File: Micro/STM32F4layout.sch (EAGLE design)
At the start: 38 parts, among them Q1 ASF, U1 LM1085IS-3.3

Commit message: Finished Power Layout, added pin header, added USB
finished list from Luke/Sam Conversation
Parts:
- removed SV2, SV3: (no value), Connectors:FE18-2
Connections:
- removed net N$8: RN1A.2
- removed net N$9: RN1B.2
- new net ETH_MDC: SV1.31
- net +3V3: now also SV1.4, U1.OUT, U1.VOUT; no longer C14.2
- net +5V: now also SV1.2
- net CAN1_RX: now also RN1A.2, SV1.1
- net CAN1_TX: now also RN1B.2, SV1.3
- net CAN2_RX: now also SV1.5
- net CAN2_TX: now also SV1.7
- net ETH_CRS_DV: now also SV1.25
- net ETH_MDIO: now also SV1.23
- net ETH_REF_CLK: now also SV1.21
- net ETH_RXD0: now also SV1.27
- net ETH_RXD1: now also SV1.29
- net ETH_TXD0: now also SV1.9
- net ETH_TXD1: now also SV1.11
- net ETH_TX_EN: now also SV1.13
- net GND: now also SV1.12, SV1.6, SV1.8, U1.ADJ/GND
- net I2C_SCL: now also SV1.17
- net I2C_SDA: now also SV1.19
- net OSC_IN: now also SV1.15
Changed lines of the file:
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@@
 <part name="GND16" library="SparkFun-Aesthetics" deviceset="GND" device=""/>
 <part name="SV1" library="Connectors" deviceset="FE18-2" device=""/>
-<part name="SV2" library="Connectors" deviceset="FE18-2" device=""/>
-<part name="SV3" library="Connectors" deviceset="FE18-2" device=""/>
+<part name="GND17" library="SparkFun-Aesthetics" deviceset="GND" device=""/>
+<part name="+3V8" library="supply1" deviceset="+3V3" device=""/>
 </parts>
 <sheets>
@@
 <instance part="GND16" gate="1" x="111.76" y="-121.92"/>
 <instance part="SV1" gate="G$1" x="160.02" y="-162.56"/>
-<instance part="SV2" gate="G$1" x="160.02" y="-215.9"/>
-<instance part="SV3" gate="G$1" x="160.02" y="-269.24"/>
+<instance part="GND17" gate="1" x="-439.42" y="-261.62"/>
+<instance part="+3V8" gate="G$1" x="-386.08" y="-226.06"/>
 </instances>
 <busses>
@@
 <junction x="106.68" y="-114.3"/>
 </segment>
+<segment>
+<pinref part="GND17" gate="1" pin="GND"/>
+<pinref part="U1" gate="A" pin="ADJ/GND"/>
+<wire x1="-439.42" y1="-259.08" x2="-439.42" y2="-248.92" width="0.1524" layer="91"/>
+</segment>
+<segment>
+<pinref part="SV1" gate="G$1" pin="6"/>
+<wire x1="167.64" y1="-180.34" x2="172.72" y2="-180.34" width="0.1524" layer="91"/>
+<label x="170.18" y="-180.34" size="1.778" layer="95"/>
+</segment>
+<segment>
+<pinref part="SV1" gate="G$1" pin="8"/>
+<wire x1="167.64" y1="-177.8" x2="172.72" y2="-177.8" width="0.1524" layer="91"/>
+<label x="170.18" y="-177.8" size="1.778" layer="95"/>
+</segment>
+<segment>
+<wire x1="165.1" y1="-175.26" x2="172.72" y2="-175.26" width="0.1524" layer="91"/>
+<label x="170.18" y="-175.26" size="1.778" layer="95"/>
+</segment>
+<segment>
+<pinref part="SV1" gate="G$1" pin="12"/>
+<wire x1="167.64" y1="-172.72" x2="172.72" y2="-172.72" width="0.1524" layer="91"/>
+<label x="170.18" y="-172.72" size="1.778" layer="95"/>
+</segment>
 </net>
 <net name="+3V3" class="0">
@@
 <junction x="-259.08" y="-20.32"/>
 <pinref part="U$1" gate="G$6" pin="VDD3"/>
-<pinref part="C14" gate="G$1" pin="2"/>
 <wire x1="-264.16" y1="-15.24" x2="-259.08" y2="-15.24" width="0.1524" layer="91"/>
-<wire x1="-259.08" y1="-15.24" x2="-238.76" y2="-15.24" width="0.1524" layer="91"/>
-<wire x1="-238.76" y1="-15.24" x2="-238.76" y2="-2.54" width="0.1524" layer="91"/>
-<junction x="-238.76" y="-15.24"/>
+<wire x1="-259.08" y1="-15.24" x2="-220.98" y2="-15.24" width="0.1524" layer="91"/>
 <wire x1="-259.08" y1="-20.32" x2="-259.08" y2="-15.24" width="0.1524" layer="91"/>
 <junction x="-259.08" y="-15.24"/>
@@
 <junction x="-261.62" y="-5.08"/>
 <wire x1="-259.08" y1="-10.16" x2="-259.08" y2="-5.08" width="0.1524" layer="91"/>
-<wire x1="-238.76" y1="-15.24" x2="-220.98" y2="-15.24" width="0.1524" layer="91"/>
 <pinref part="C13" gate="G$1" pin="1"/>
 <wire x1="-259.08" y1="-20.32" x2="-241.3" y2="-20.32" width="0.1524" layer="91"/>
@@
 <wire x1="88.9" y1="86.36" x2="88.9" y2="83.82" width="0.1524" layer="91"/>
 </segment>
+<segment>
+<pinref part="+3V8" gate="G$1" pin="+3V3"/>
+<wire x1="-398.78" y1="-243.84" x2="-386.08" y2="-243.84" width="0.1524" layer="91"/>
+<pinref part="U1" gate="A" pin="VOUT"/>
+<wire x1="-386.08" y1="-243.84" x2="-386.08" y2="-228.6" width="0.1524" layer="91"/>
+<wire x1="-398.78" y1="-246.38" x2="-386.08" y2="-246.38" width="0.1524" layer="91"/>
+<wire x1="-386.08" y1="-246.38" x2="-386.08" y2="-243.84" width="0.1524" layer="91"/>
+<pinref part="U1" gate="A" pin="OUT"/>
+<wire x1="-401.32" y1="-243.84" x2="-398.78" y2="-243.84" width="0.1524" layer="91"/>
+<junction x="-398.78" y="-243.84"/>
+</segment>
+<segment>
+<pinref part="SV1" gate="G$1" pin="4"/>
+<wire x1="167.64" y1="-182.88" x2="172.72" y2="-182.88" width="0.1524" layer="91"/>
+<label x="170.18" y="-182.88" size="1.778" layer="95"/>
+</segment>
 </net>
 <net name="N$3" class="0">
@@
 <label x="-43.18" y="78.74" size="1.778" layer="95"/>
 </segment>
+<segment>
+<pinref part="SV1" gate="G$1" pin="17"/>
+<wire x1="152.4" y1="-165.1" x2="149.86" y2="-165.1" width="0.1524" layer="91"/>
+<label x="142.24" y="-165.1" size="1.778" layer="95"/>
+</segment>
 </net>
 <net name="I2C_SDA" class="0">
@@
 <label x="93.98" y="73.66" size="1.778" layer="95"/>
 </segment>
+<segment>
+<pinref part="SV1" gate="G$1" pin="19"/>
+<wire x1="152.4" y1="-162.56" x2="149.86" y2="-162.56" width="0.1524" layer="91"/>
+<label x="142.24" y="-162.56" size="1.778" layer="95"/>
+</segment>
 </net>
 <net name="N$6" class="0">
@@
 <pinref part="RN1" gate="A" pin="1"/>
 <wire x1="-485.14" y1="-271.78" x2="-464.82" y2="-271.78" width="0.1524" layer="91"/>
-</segment>
-</net>
-<net name="N$8" class="0">
-<segment>
-<pinref part="RN1" gate="A" pin="2"/>
-<wire x1="-454.66" y1="-271.78" x2="-452.12" y2="-271.78" width="0.1524" layer="91"/>
-</segment>
-</net>
-<net name="N$9" class="0">
-<segment>
-<pinref part="RN1" gate="B" pin="2"/>
-<wire x1="-454.66" y1="-276.86" x2="-452.12" y2="-276.86" width="0.1524" layer="91"/>
 </segment>
 </net>
@@
 <junction x="-464.82" y="-243.84"/>
 </segment>
+<segment>
+<pinref part="SV1" gate="G$1" pin="2"/>
+<wire x1="167.64" y1="-185.42" x2="172.72" y2="-185.42" width="0.1524" layer="91"/>
+<label x="170.18" y="-185.42" size="1.778" layer="95"/>
+</segment>
 </net>
 <net name="N$5" class="0">
@@
 <wire x1="-60.96" y1="-160.02" x2="-43.18" y2="-160.02" width="0.1524" layer="91"/>
 <label x="-55.88" y="-160.02" size="1.778" layer="95"/>
+</segment>
+<segment>
+<pinref part="SV1" gate="G$1" pin="15"/>
+<wire x1="152.4" y1="-167.64" x2="149.86" y2="-167.64" width="0.1524" layer="91"/>
+<label x="142.24" y="-167.64" size="1.778" layer="95"/>
 </segment>
 </net>
@@
 <label x="-63.5" y="58.42" size="1.778" layer="95"/>
 </segment>
+<segment>
+<pinref part="RN1" gate="B" pin="2"/>
+<wire x1="-454.66" y1="-276.86" x2="-452.12" y2="-276.86" width="0.1524" layer="91"/>
+</segment>
+<segment>
+<pinref part="SV1" gate="G$1" pin="3"/>
+<wire x1="152.4" y1="-182.88" x2="149.86" y2="-182.88" width="0.1524" layer="91"/>
+<label x="142.24" y="-182.88" size="1.778" layer="95"/>
+</segment>
 </net>
 <net name="N$13" class="0">
@@
 <label x="-66.04" y="114.3" size="1.778" layer="95"/>
 </segment>
+<segment>
+<pinref part="SV1" gate="G$1" pin="21"/>
+<wire x1="152.4" y1="-160.02" x2="149.86" y2="-160.02" width="0.1524" layer="91"/>
+<label x="137.16" y="-160.02" size="1.778" layer="95"/>
+</segment>
 </net>
 <net name="ETH_MDIO" class="0">
@@
 <label x="-66.04" y="109.22" size="1.778" layer="95"/>
 </segment>
+<segment>
+<pinref part="SV1" gate="G$1" pin="23"/>
+<wire x1="152.4" y1="-157.48" x2="149.86" y2="-157.48" width="0.1524" layer="91"/>
+<label x="139.7" y="-157.48" size="1.778" layer="95"/>
+</segment>
 </net>
 <net name="ETH_CRS_DV" class="0">
@@
 <label x="-68.58" y="83.82" size="1.778" layer="95"/>
 </segment>
+<segment>
+<pinref part="SV1" gate="G$1" pin="25"/>
+<wire x1="152.4" y1="-154.94" x2="149.86" y2="-154.94" width="0.1524" layer="91"/>
+<label x="137.16" y="-154.94" size="1.778" layer="95"/>
+</segment>
 </net>
 <net name="ETH_RXD0" class="0">
@@
 <label x="73.66" y="99.06" size="1.778" layer="95"/>
 </segment>
+<segment>
+<pinref part="SV1" gate="G$1" pin="27"/>
+<wire x1="152.4" y1="-152.4" x2="149.86" y2="-152.4" width="0.1524" layer="91"/>
+<label x="139.7" y="-152.4" size="1.778" layer="95"/>
+</segment>
 </net>
 <net name="ETH_RXD1" class="0">
@@
 <label x="73.66" y="93.98" size="1.778" layer="95"/>
 </segment>
+<segment>
+<pinref part="SV1" gate="G$1" pin="29"/>
+<wire x1="152.4" y1="-149.86" x2="149.86" y2="-149.86" width="0.1524" layer="91"/>
+<label x="139.7" y="-149.86" size="1.778" layer="95"/>
+</segment>
 </net>
 <net name="BUCK_ON/OFF" class="0">
@@
 <label x="-58.42" y="-93.98" size="1.778" layer="95"/>
 </segment>
+<segment>
+<pinref part="SV1" gate="G$1" pin="13"/>
+<wire x1="152.4" y1="-170.18" x2="149.86" y2="-170.18" width="0.1524" layer="91"/>
+<label x="142.24" y="-170.18" size="1.778" layer="95"/>
+</segment>
 </net>
 <net name="ETH_TXD1" class="0">
@@
 <label x="-58.42" y="-104.14" size="1.778" layer="95"/>
 </segment>
+<segment>
+<pinref part="SV1" gate="G$1" pin="11"/>
+<wire x1="152.4" y1="-172.72" x2="149.86" y2="-172.72" width="0.1524" layer="91"/>
+<label x="142.24" y="-172.72" size="1.778" layer="95"/>
+</segment>
 </net>
 <net name="ETH_TXD0" class="0">
@@
 <label x="-58.42" y="-99.06" size="1.778" layer="95"/>
 </segment>
+<segment>
+<pinref part="SV1" gate="G$1" pin="9"/>
+<wire x1="152.4" y1="-175.26" x2="149.86" y2="-175.26" width="0.1524" layer="91"/>
+<label x="142.24" y="-175.26" size="1.778" layer="95"/>
+</segment>
 </net>
 <net name="CAN2_TX" class="0">
@@
 <label x="-93.98" y="-330.2" size="1.778" layer="95"/>
 </segment>
+<segment>
+<pinref part="SV1" gate="G$1" pin="7"/>
+<wire x1="152.4" y1="-177.8" x2="149.86" y2="-177.8" width="0.1524" layer="91"/>
+<label x="142.24" y="-177.8" size="1.778" layer="95"/>
+</segment>
 </net>
 <net name="CAN2_RX" class="0">
@@
 <label x="-93.98" y="-335.28" size="1.778" layer="95"/>
 </segment>
+<segment>
+<pinref part="SV1" gate="G$1" pin="5"/>
+<wire x1="152.4" y1="-180.34" x2="149.86" y2="-180.34" width="0.1524" layer="91"/>
+<label x="142.24" y="-180.34" size="1.778" layer="95"/>
+</segment>
 </net>
 <net name="CAN1_RX" class="0">
@@
 <label x="-96.52" y="-256.54" size="1.778" layer="95"/>
 </segment>
-</net>
+<segment>
+<pinref part="RN1" gate="A" pin="2"/>
+<wire x1="-454.66" y1="-271.78" x2="-452.12" y2="-271.78" width="0.1524" layer="91"/>
+</segment>
+<segment>
+<pinref part="SV1" gate="G$1" pin="1"/>
+<wire x1="152.4" y1="-185.42" x2="149.86" y2="-185.42" width="0.1524" layer="91"/>
+<label x="142.24" y="-185.42" size="1.778" layer="95"/>
+</segment>
+</net>
+<net name="ETH_MDC" class="0">
+<segment>
+<pinref part="SV1" gate="G$1" pin="31"/>
+<wire x1="152.4" y1="-147.32" x2="149.86" y2="-147.32" width="0.1524" layer="91"/>
+<label x="139.7" y="-147.32" size="1.778" layer="95"/>
+</segment>
+</net>

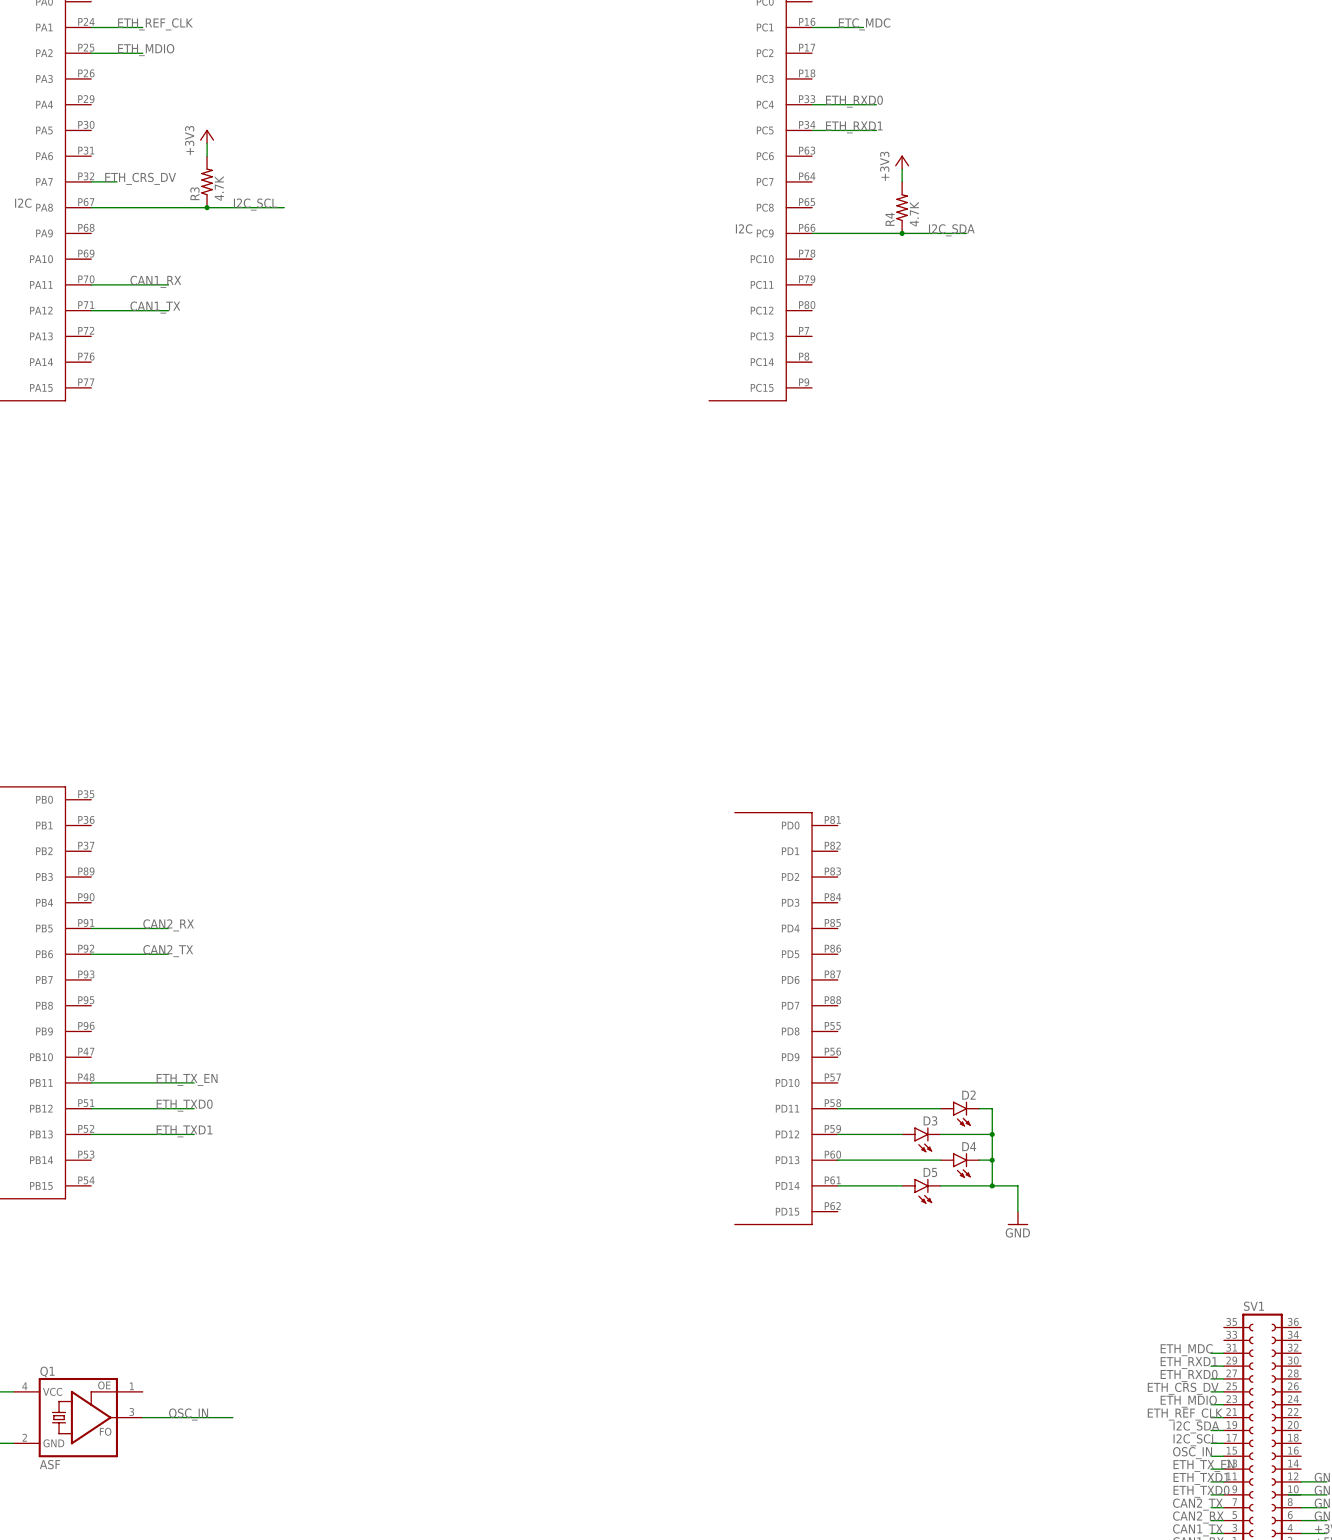
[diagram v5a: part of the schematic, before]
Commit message: Added some of needed additional circuits
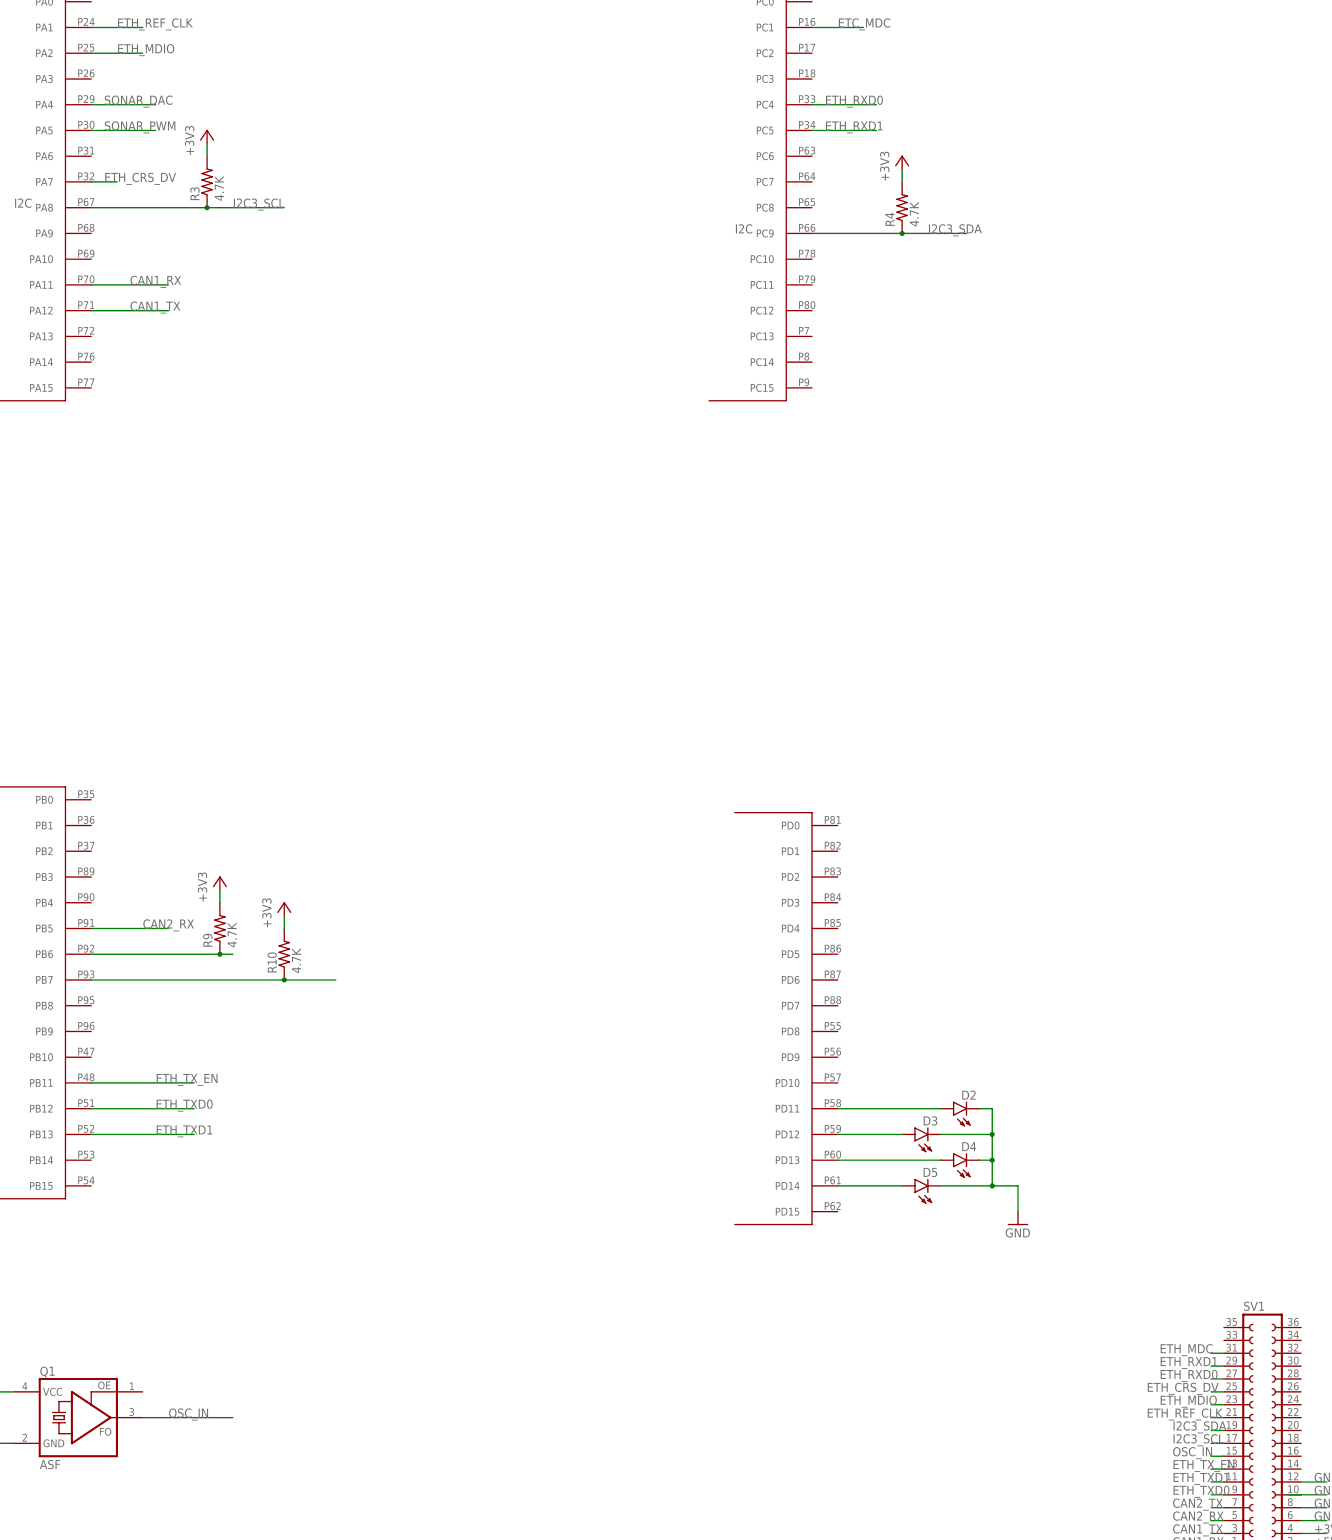
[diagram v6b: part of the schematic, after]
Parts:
- added R10, R9: 4.7K, SparkFun-Passives:RESISTOR0603-RES
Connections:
- net I2C_SCL renamed I2C3_SCL
- net I2C_SDA renamed I2C3_SDA
- new net I2C1_SCL: R9.1, U$1G$2.PB6
- new net I2C1_SDA: R10.1, U$1G$2.PB7
- new net SONAR_DAC: U$1G$1.PA4
- new net SONAR_PWM: U$1G$1.PA5
- net +3V3: now also R10.2, R9.2
- net CAN2_TX: no longer U$1G$2.PB6
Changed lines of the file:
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@@
 <part name="GND17" library="SparkFun-Aesthetics" deviceset="GND" device=""/>
 <part name="+3V8" library="supply1" deviceset="+3V3" device=""/>
+<part name="R9" library="SparkFun-Passives" deviceset="RESISTOR" device="0603-RES" value="4.7K"/>
+<part name="+3V9" library="supply1" deviceset="+3V3" device=""/>
+<part name="R10" library="SparkFun-Passives" deviceset="RESISTOR" device="0603-RES" value="4.7K"/>
+<part name="+3V10" library="supply1" deviceset="+3V3" device=""/>
 </parts>
 <sheets>
@@
 <instance part="GND17" gate="1" x="-439.42" y="-261.62"/>
 <instance part="+3V8" gate="G$1" x="-386.08" y="-226.06"/>
+<instance part="R9" gate="G$1" x="-45.72" y="-63.5" rot="R90"/>
+<instance part="+3V9" gate="G$1" x="-45.72" y="-53.34"/>
+<instance part="R10" gate="G$1" x="-33.02" y="-68.58" rot="R90"/>
+<instance part="+3V10" gate="G$1" x="-33.02" y="-58.42"/>
 </instances>
 <busses>
@@
 <label x="170.18" y="-182.88" size="1.778" layer="95"/>
 </segment>
+<segment>
+<pinref part="R9" gate="G$1" pin="2"/>
+<pinref part="+3V9" gate="G$1" pin="+3V3"/>
+<wire x1="-45.72" y1="-55.88" x2="-45.72" y2="-58.42" width="0.1524" layer="91"/>
+</segment>
+<segment>
+<pinref part="R10" gate="G$1" pin="2"/>
+<pinref part="+3V10" gate="G$1" pin="+3V3"/>
+<wire x1="-33.02" y1="-60.96" x2="-33.02" y2="-63.5" width="0.1524" layer="91"/>
+</segment>
 </net>
 <net name="N$3" class="0">
@@
 </segment>
 </net>
-<net name="I2C_SCL" class="0">
+<net name="I2C3_SCL" class="0">
 <segment>
 <pinref part="U$1" gate="G$1" pin="PA8"/>
@@
 </segment>
 </net>
-<net name="I2C_SDA" class="0">
+<net name="I2C3_SDA" class="0">
 <segment>
 <pinref part="U$1" gate="G$3" pin="PC9"/>
@@
 <net name="CAN2_TX" class="0">
 <segment>
-<pinref part="U$1" gate="G$2" pin="PB6"/>
-<wire x1="-71.12" y1="-68.58" x2="-55.88" y2="-68.58" width="0.1524" layer="91"/>
-<label x="-60.96" y="-68.58" size="1.778" layer="95"/>
-</segment>
-<segment>
 <pinref part="U$6" gate="G$1" pin="TXD"/>
 <wire x1="-86.36" y1="-330.2" x2="-91.44" y2="-330.2" width="0.1524" layer="91"/>
@@
 </segment>
 </net>
+<net name="SONAR_PWM" class="0">
+<segment>
+<pinref part="U$1" gate="G$1" pin="PA5"/>
+<wire x1="-71.12" y1="93.98" x2="-58.42" y2="93.98" width="0.1524" layer="91"/>
+<label x="-68.58" y="93.98" size="1.778" layer="95"/>
+</segment>
+</net>
+<net name="SONAR_DAC" class="0">
+<segment>
+<pinref part="U$1" gate="G$1" pin="PA4"/>
+<wire x1="-71.12" y1="99.06" x2="-58.42" y2="99.06" width="0.1524" layer="91"/>
+<label x="-68.58" y="99.06" size="1.778" layer="95"/>
+</segment>
+</net>
+<net name="I2C1_SDA" class="0">
+<segment>
+<pinref part="U$1" gate="G$2" pin="PB7"/>
+<wire x1="-71.12" y1="-73.66" x2="-33.02" y2="-73.66" width="0.1524" layer="91"/>
+<pinref part="R10" gate="G$1" pin="1"/>
+<junction x="-33.02" y="-73.66"/>
+<wire x1="-33.02" y1="-73.66" x2="-22.86" y2="-73.66" width="0.1524" layer="91"/>
+</segment>
+</net>
+<net name="I2C1_SCL" class="0">
+<segment>
+<pinref part="U$1" gate="G$2" pin="PB6"/>
+<wire x1="-71.12" y1="-68.58" x2="-45.72" y2="-68.58" width="0.1524" layer="91"/>
+<pinref part="R9" gate="G$1" pin="1"/>
+<junction x="-45.72" y="-68.58"/>
+<wire x1="-45.72" y1="-68.58" x2="-43.18" y2="-68.58" width="0.1524" layer="91"/>
+</segment>
+</net>
